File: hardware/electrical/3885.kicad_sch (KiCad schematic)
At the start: 0 parts

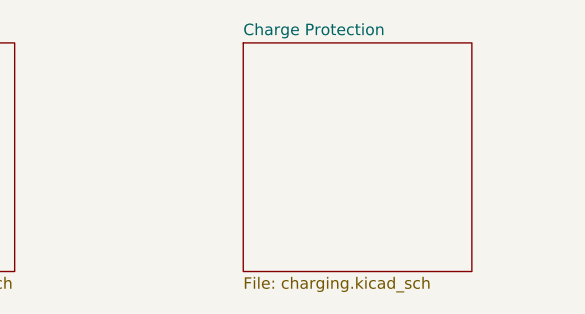
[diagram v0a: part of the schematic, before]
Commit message: Add camera module sheet to schematic hierarchy
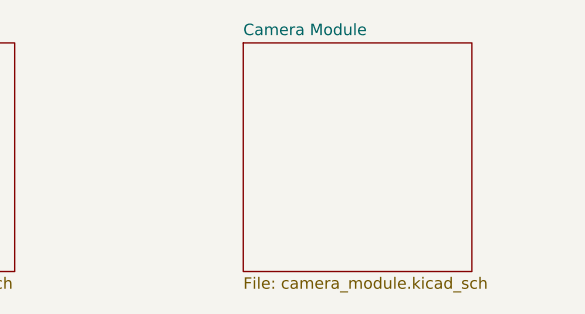
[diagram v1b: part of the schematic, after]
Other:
- sheet Charge Protection renamed Camera Module
- sheet Camera Module: file charging.kicad_sch -> camera_module.kicad_sch
